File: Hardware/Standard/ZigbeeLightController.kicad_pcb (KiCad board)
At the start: 2 copper layers, 159 x 71 mm, 108 parts, among them J1 M20-7870346, J2 1935268, J3 1935268, J4 1935161, Q1 2N7002, Q10 FDMS7682, Q11 FDMS7682, Q12 FDMS7682, Q13 FDMS7682, Q14 FDMS7682, Q2 2N7002, Q3 FDMS7682, Q4 FDMS7682, Q5 FDMS7682, Q6 FDMS7682, Q7 FDMS7682, Q8 FDMS7682, Q9 FDMS7682, SW1 SW_Push, U1 MCP16301, U10 ZXGD3009DY, U11 ZXGD3009DY, U12 ZXGD3009DY, U13 ZXGD3009DY, U14 ZXGD3009DY, U15 ZXGD3009DY, U16 ZXGD3009DY, U2 AP2120N-3.3, U3 JN5168-001-M00, U4 PCA9685, U5 ZXGD3009DY, U6 ZXGD3009DY, U7 ZXGD3009DY, U8 ZXGD3009DY, U9 ZXGD3009DY

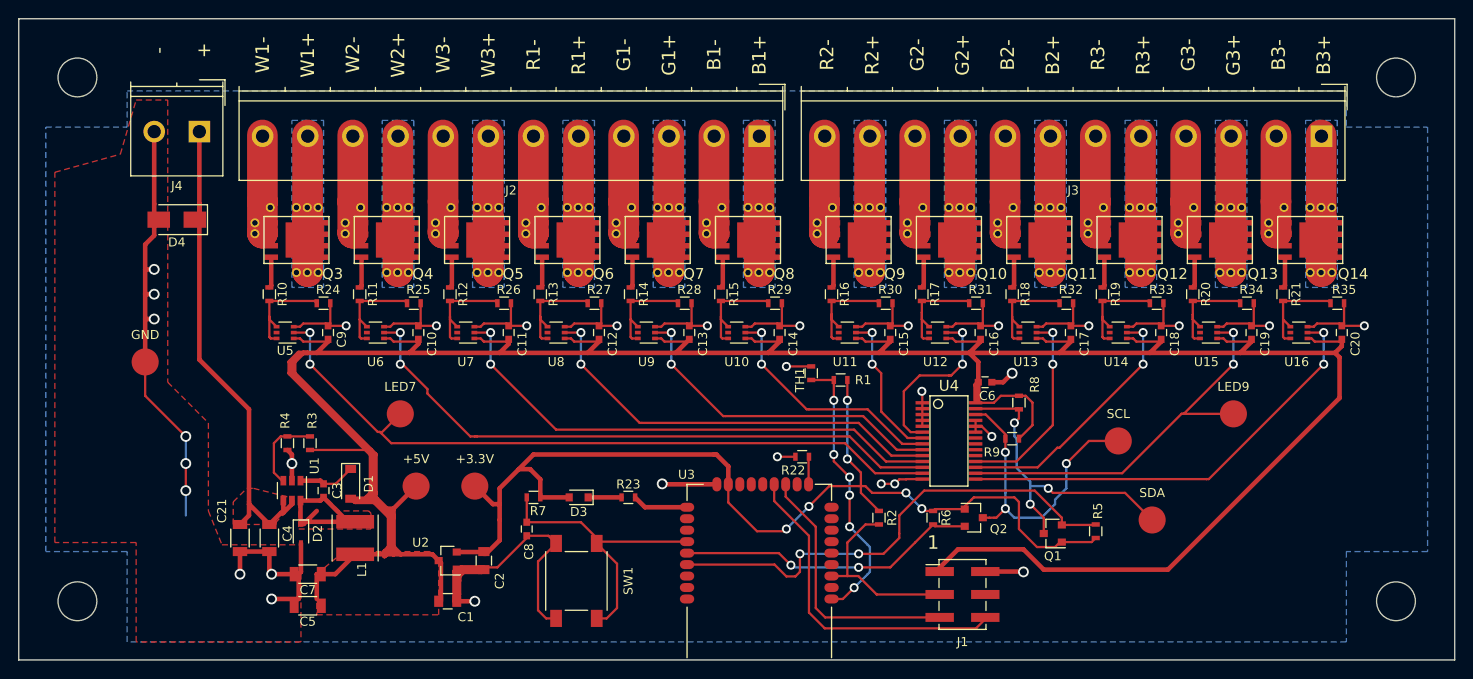
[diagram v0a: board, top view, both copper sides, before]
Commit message: Standard hardware bugfixes: changed BOM to use correct 0603 part instead of 0402 part, widened pad for D3, changed R2 to 10k to reduce line item count, filling top layer
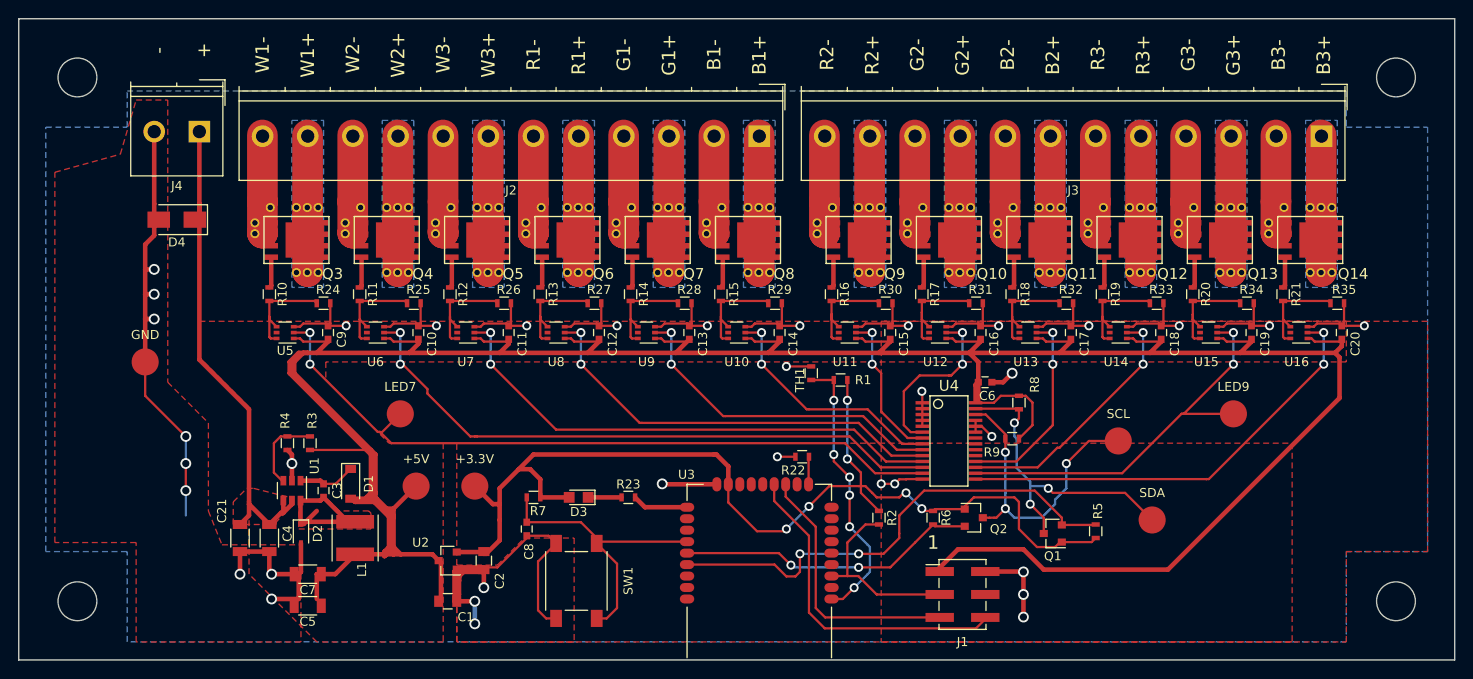
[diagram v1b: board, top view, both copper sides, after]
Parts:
- D3: footprint Diodes_SMD:D_0805 -> zll_lib:D_0805_LED
- R2: value 100k -> 10k
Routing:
- net GND: track 412.3 -> 421.8 mm, vias 32 -> 36
- added copper zone on F.Cu, net +3V3

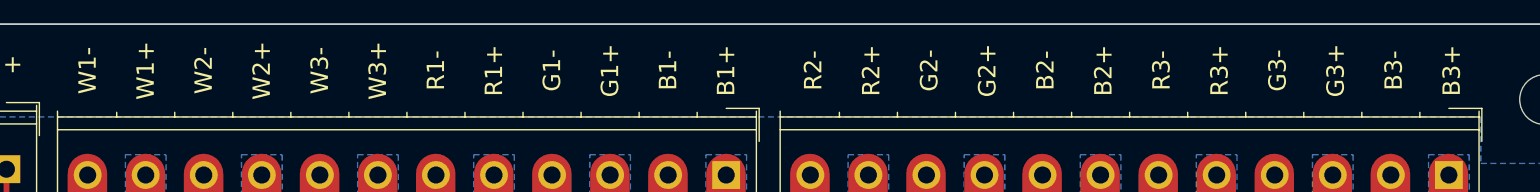
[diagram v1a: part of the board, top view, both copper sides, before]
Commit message: Fixing PCB fill issue, using - and K for LED terminals
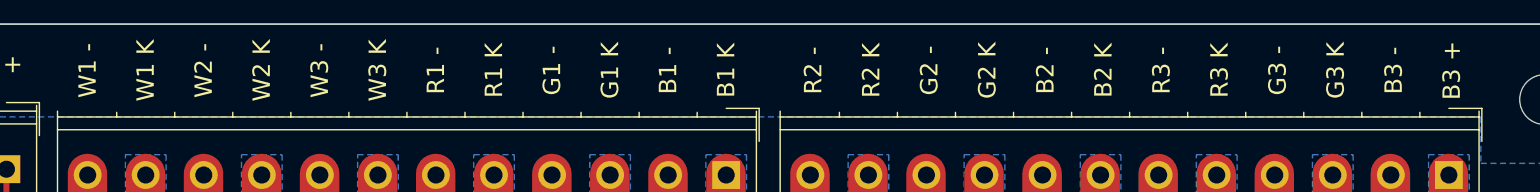
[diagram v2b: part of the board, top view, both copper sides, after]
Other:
- board text added: "B1 -"
- board text added: "B1 K"
- board text added: "B2 -"
- board text added: "B2 K"
- board text added: "B3 +"
- board text added: "B3 -"
- board text added: "G1 -"
- board text added: "G1 K"
- board text added: "G2 -"
- board text added: "G2 K"
- board text added: "G3 -"
- board text added: "G3 K"
- board text added: "R1 -"
- board text added: "R1 K"
- board text added: "R2 -"
- board text added: "R2 K"
- board text added: "R3 -"
- board text added: "R3 K"
- board text added: "W1 -"
- board text added: "W1 K"
- board text added: "W2 -"
- board text added: "W2 K"
- board text added: "W3 -"
- board text added: "W3 K"
- board text removed: "B1+"
- board text removed: "B1-"
- board text removed: "B2+"
- board text removed: "B2-"
- board text removed: "B3+"
- board text removed: "B3-"
- board text removed: "G1+"
- board text removed: "G1-"
- board text removed: "G2+"
- board text removed: "G2-"
- board text removed: "G3+"
- board text removed: "G3-"
- board text removed: "R1+"
- board text removed: "R1-"
- board text removed: "R2+"
- board text removed: "R2-"
- board text removed: "R3+"
- board text removed: "R3-"
- board text removed: "W1+"
- board text removed: "W1-"
- board text removed: "W2+"
- board text removed: "W2-"
- board text removed: "W3+"
- board text removed: "W3-"
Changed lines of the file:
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@@
   )
   (setup
-    (last_trace_width 0.508)
+    (last_trace_width 0.254)
     (user_trace_width 0.508)
     (user_trace_width 3.4)
     (trace_clearance 0.2)
-    (zone_clearance 1)
+    (zone_clearance 0.762)
     (zone_45_only yes)
     (trace_min 0.2)
@@
     (effects (font (size 1.5 1.5) (thickness 0.3)))
   )
-  (gr_text B3+ (at 211.5 30.5 90) (layer F.SilkS)
+  (gr_text "B3 +" (at 211.5 30.5 90) (layer F.SilkS)
     (effects (font (size 1.5 1.5) (thickness 0.3)))
   )
-  (gr_text B3- (at 206.5 30.5 90) (layer F.SilkS)
+  (gr_text "B3 -" (at 206.5 30.5 90) (layer F.SilkS)
     (effects (font (size 1.5 1.5) (thickness 0.3)))
   )
-  (gr_text G3+ (at 201.5 30.5 90) (layer F.SilkS)
+  (gr_text "G3 K" (at 201.5 30.5 90) (layer F.SilkS)
     (effects (font (size 1.5 1.5) (thickness 0.3)))
   )
-  (gr_text G3- (at 196.5 30.5 90) (layer F.SilkS)
+  (gr_text "G3 -" (at 196.5 30.5 90) (layer F.SilkS)
     (effects (font (size 1.5 1.5) (thickness 0.3)))
   )
-  (gr_text R3+ (at 191.5 30.5 90) (layer F.SilkS)
+  (gr_text "R3 K" (at 191.5 30.5 90) (layer F.SilkS)
     (effects (font (size 1.5 1.5) (thickness 0.3)))
   )
-  (gr_text R3- (at 186.5 30.5 90) (layer F.SilkS)
+  (gr_text "R3 -" (at 186.5 30.5 90) (layer F.SilkS)
     (effects (font (size 1.5 1.5) (thickness 0.3)))
   )
-  (gr_text B2+ (at 181.5 30.5 90) (layer F.SilkS)
+  (gr_text "B2 K" (at 181.5 30.5 90) (layer F.SilkS)
     (effects (font (size 1.5 1.5) (thickness 0.3)))
   )
-  (gr_text B2- (at 176.5 30.5 90) (layer F.SilkS)
+  (gr_text "B2 -" (at 176.5 30.5 90) (layer F.SilkS)
     (effects (font (size 1.5 1.5) (thickness 0.3)))
   )
-  (gr_text G2+ (at 171.5 30.5 90) (layer F.SilkS)
+  (gr_text "G2 K" (at 171.5 30.5 90) (layer F.SilkS)
     (effects (font (size 1.5 1.5) (thickness 0.3)))
   )
-  (gr_text G2- (at 166.5 30.5 90) (layer F.SilkS)
+  (gr_text "G2 -" (at 166.5 30.5 90) (layer F.SilkS)
     (effects (font (size 1.5 1.5) (thickness 0.3)))
   )
-  (gr_text R2+ (at 161.5 30.5 90) (layer F.SilkS)
+  (gr_text "R2 K" (at 161.5 30.5 90) (layer F.SilkS)
     (effects (font (size 1.5 1.5) (thickness 0.3)))
   )
-  (gr_text R2- (at 156.5 30.5 90) (layer F.SilkS)
+  (gr_text "R2 -" (at 156.5 30.5 90) (layer F.SilkS)
     (effects (font (size 1.5 1.5) (thickness 0.3)))
   )
-  (gr_text B1+ (at 149 30.5 90) (layer F.SilkS)
+  (gr_text "B1 K" (at 149 30.5 90) (layer F.SilkS)
     (effects (font (size 1.5 1.5) (thickness 0.3)))
   )
-  (gr_text B1- (at 144 30.5 90) (layer F.SilkS)
+  (gr_text "B1 -" (at 144 30.5 90) (layer F.SilkS)
     (effects (font (size 1.5 1.5) (thickness 0.3)))
   )
-  (gr_text G1+ (at 139 30.5 90) (layer F.SilkS)
+  (gr_text "G1 K" (at 139 30.5 90) (layer F.SilkS)
     (effects (font (size 1.5 1.5) (thickness 0.3)))
   )
-  (gr_text G1- (at 134 30.5 90) (layer F.SilkS)
+  (gr_text "G1 -" (at 134 30.5 90) (layer F.SilkS)
     (effects (font (size 1.5 1.5) (thickness 0.3)))
   )
-  (gr_text R1+ (at 129 30.5 90) (layer F.SilkS)
+  (gr_text "R1 K" (at 129 30.5 90) (layer F.SilkS)
     (effects (font (size 1.5 1.5) (thickness 0.3)))
   )
-  (gr_text R1- (at 124 30.5 90) (layer F.SilkS)
+  (gr_text "R1 -" (at 124 30.5 90) (layer F.SilkS)
     (effects (font (size 1.5 1.5) (thickness 0.3)))
   )
-  (gr_text W3+ (at 119 30.5 90) (layer F.SilkS)
+  (gr_text "W3 K" (at 119 30.5 90) (layer F.SilkS)
     (effects (font (size 1.5 1.5) (thickness 0.3)))
   )
-  (gr_text W3- (at 114 30.5 90) (layer F.SilkS)
+  (gr_text "W3 -" (at 114 30.5 90) (layer F.SilkS)
     (effects (font (size 1.5 1.5) (thickness 0.3)))
   )
-  (gr_text W2+ (at 109 30.5 90) (layer F.SilkS)
+  (gr_text "W2 K" (at 109 30.5 90) (layer F.SilkS)
     (effects (font (size 1.5 1.5) (thickness 0.3)))
   )
-  (gr_text W2- (at 104 30.5 90) (layer F.SilkS)
+  (gr_text "W2 -" (at 104 30.5 90) (layer F.SilkS)
     (effects (font (size 1.5 1.5) (thickness 0.3)))
   )
-  (gr_text W1+ (at 99 30.5 90) (layer F.SilkS)
+  (gr_text "W1 K" (at 99 30.5 90) (layer F.SilkS)
     (effects (font (size 1.5 1.5) (thickness 0.3)))
   )
-  (gr_text W1- (at 94 30.5 90) (layer F.SilkS)
+  (gr_text "W1 -" (at 94 30.5 90) (layer F.SilkS)
     (effects (font (size 1.5 1.5) (thickness 0.3)))
   )
@@
   (segment (start 117.5 91) (end 115.25 91) (width 0.508) (layer F.Cu) (net 1))
   (via (at 117.5 93.5) (size 1.2) (drill 0.8) (layers F.Cu B.Cu) (net 1))
-  (segment (start 118.5 87.5) (end 118.5 89.5) (width 0.508) (layer F.Cu) (net 1) (status 400000))
+  (segment (start 118.5 87.5) (end 118.5 89.5) (width 0.508) (layer F.Cu) (net 1))
   (via (at 118.5 89.5) (size 1.2) (drill 0.8) (layers F.Cu B.Cu) (net 1))
   (segment (start 178.25 92.75) (end 178.25 90.25) (width 0.508) (layer F.Cu) (net 1))
@@
   )
   (zone (net 6) (net_name /V_IN) (layer F.Cu) (hatch edge 0.508)
+    (priority 2)
     (connect_pads yes (clearance 0.762))
     (min_thickness 0.254)
